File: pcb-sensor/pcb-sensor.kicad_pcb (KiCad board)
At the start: 2 copper layers, 84 x 84 mm, 13 parts, among them J1 Conn_02x06_Counter_Clockwise, J2 Conn_01x10, U1 4N25, U2 LT1962-5

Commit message: sensor pcb
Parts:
- added D3: D, Diode_SMD:D_1206_3216Metric_Pad1.42x1.75mm_HandSolder, F.Cu at (135.0, 98.5)
- added J3: Conn_01x02, Connector_PinSocket_2.54mm:PinSocket_2x01_P2.54mm_Vertical, F.Cu at (176.6, 103.3)
- added R10: R, Resistor_SMD:R_1206_3216Metric_Pad1.30x1.75mm_HandSolder, F.Cu at (144.0, 81.5)
- added R11: R, Resistor_SMD:R_1206_3216Metric_Pad1.30x1.75mm_HandSolder, F.Cu at (160.0, 88.5)
- added R12: R, Resistor_SMD:R_1206_3216Metric_Pad1.30x1.75mm_HandSolder, F.Cu at (178.6, 97.3)
- added R7: R, Resistor_SMD:R_1206_3216Metric_Pad1.30x1.75mm_HandSolder, F.Cu at (148.0, 72.5)
- added R8: R, Resistor_SMD:R_1206_3216Metric_Pad1.30x1.75mm_HandSolder, F.Cu at (143.9, 65.5)
- added R9: R, Resistor_SMD:R_1206_3216Metric_Pad1.30x1.75mm_HandSolder, F.Cu at (158.9, 65.5)
- added U3: 4N35, footprints:4N35S, F.Cu at (153.5, 69.0)
- added U4: 4N35, footprints:4N35S, F.Cu at (138.5, 85.0)
- added U5: TLSM, footprints:TLSM, F.Cu at (187.5, 100.3)
- J2: value Conn_01x10 -> Conn_01x12; footprint Connector_JST:JST_XH_S10B-XH-A_1x10_P2.50mm_Horizontal -> Connector_PinHeader_2.54mm:PinHeader_1x12_P2.54mm_Vertical
- U1: value 4N25 -> LM340MP; footprint Package_DIP:DIP-6_W7.62mm -> Package_TO_SOT_SMD:SOT-223
- U2: value LT1962-5 -> 4N35; footprint Package_SO:MSOP-8_3x3mm_P0.65mm -> footprints:4N35S
- moved U1 65.1 mm to (177.8, 116.0)
- moved U2 63.8 mm to (138.5, 69.0), turned to 0 degrees
- moved C1 29.2 mm to (135.0, 104.6)
- moved R6 28.7 mm to (131.0, 104.5)
- moved J2 28.1 mm to (136.0, 122.0), turned to 90 degrees
- moved R3 23.7 mm to (152.0, 88.5), turned to 270 degrees
- moved R2 22.8 mm to (156.0, 88.5), turned to 270 degrees
- moved R5 20.9 mm to (131.0, 98.5), turned to 270 degrees
- moved R4 20.3 mm to (133.0, 72.5), turned to 270 degrees
- moved R1 17.0 mm to (133.0, 88.5)
- moved D1 14.2 mm to (131.5, 83.0), turned to 180 degrees
- moved D2 11.3 mm to (131.5, 80.0), turned to 180 degrees
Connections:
- net /TURN_SIGNAL_LEFT_12V renamed /TURN_SIGNAL_LEFT
- net /TURN_SIGNAL_RIGHT_12V renamed /TURN_SIGNAL_RIGHT
- C1 pad 1: /ADC6 -> /ADC7
- D1 pad 1: /PD5 -> Net-(D1-Pad1)
- D2 pad 1: /PD5 -> Net-(D1-Pad1)
- J1 pad 1: /HIGH_BEAM_12V -> /PD4
- J1 pad 5: /NEUTRAL_12V -> /PD2
- J1 pad 6: /PD7 -> /NEUTRAL
- J1 pad 7: +5V -> /PD1
- J2 pad 10: /TACHO_12V -> /PD2
- J2 pad 4: /HIGH_BEAM_12V -> /HIGH_BEAM
- J2 pad 5: /NEUTRAL_12V -> /NEUTRAL
- J2 pad 6: /OIL_PRESSURE_12V -> /OIL_PRESSURE
- J2 pad 9: /SPEEDO_12V -> /COIL
- R1 pad 1: /PD5 -> Net-(D1-Pad1)
- R1 pad 2: GND -> Net-(R1-Pad2)
- R2 pad 2: /NEUTRAL_12V -> /NEUTRAL
- R4 pad 1: /HIGH_BEAM_12V -> /HIGH_BEAM
- R4 pad 2: GND -> Net-(R4-Pad2)
- R5 pad 2: /ADC6 -> /ADC7
- R6 pad 1: /ADC6 -> /ADC7
- U1 pad 1: /KEY_12V -> +12V
- U1 pad 2: /TACHO_12V -> GND
- U1 pad 3: Net-(U1-Pad3) -> +5V
- U2 pad 1: +5V -> Net-(R4-Pad2)
- U2 pad 2: Net-(U2-Pad2) -> GND
- U2 pad 5: Net-(U2-Pad5) -> /PD4
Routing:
- net +5V: track 0.00 -> 96.1 mm
- net /ADC7: track 0.00 -> 56.8 mm
- net /PD4: track 0.00 -> 41.2 mm
- net /PD1: track 0.00 -> 40.3 mm
- net GND: track 3.13 -> 37.5 mm, vias 1 -> 7
- net /PD6: track 0.00 -> 34.1 mm
- net /OIL_PRESSURE_12V: track 0.00 -> 34.1 mm
- net /PD2: track 0.00 -> 25.0 mm
- net /NEUTRAL: track 0.00 -> 24.0 mm
- net /ADC6: track 10.0 -> 0.00 mm
- net /PD5: track 10.0 -> 18.1 mm
- net Net-(D1-Pad1): track 0.00 -> 6.90 mm
- net Net-(R7-Pad2): track 0.00 -> 3.00 mm
- net Net-(R4-Pad2): track 0.00 -> 3.00 mm
- net Net-(R1-Pad2): track 0.00 -> 3.00 mm
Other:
- board text added: "BATT_12V"
- board text added: "COIL"
- board text added: "GND"
- board text added: "HIGH_BEAM"
- board text added: "KEY_12V"
- board text added: "NEUTRAL"
- board text added: "OIL_PRES"
- board text added: "SPEED_5V"
- board text added: "SPEED_GND"
- board text added: "SPEED_OUT"
- board text added: "TURN_LEFT"
- board text added: "TURN_RIGHT"

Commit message: v1.0
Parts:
- moved U5 2.52 mm to (185.0, 100.0)
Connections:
- J1 pad 3: /OIL_PRESSURE_12V -> /OIL_PRESSURE
- J2 pad 2: +12V -> /HIGH_BEAM
- J2 pad 3: /KEY_12V -> /TURN_SIGNAL_RIGHT
- J2 pad 4: /HIGH_BEAM -> /TURN_SIGNAL_LEFT
- J2 pad 5: /NEUTRAL -> /KEY_12V
- J2 pad 7: /TURN_SIGNAL_RIGHT -> /NEUTRAL
- J2 pad 8: /TURN_SIGNAL_LEFT -> /COIL
- J2 pad 9: /COIL -> +12V
- R3 pad 2: /OIL_PRESSURE_12V -> /OIL_PRESSURE
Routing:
- net /OIL_PRESSURE: track 0.00 -> 74.8 mm, vias 0 -> 1
- net /KEY_12V: track 0.00 -> 67.4 mm, vias 0 -> 2
- net /HIGH_BEAM: track 0.00 -> 60.3 mm, vias 0 -> 1
- net +5V: track 96.1 -> 150.1 mm, vias 0 -> 3
- net /COIL: track 0.00 -> 52.0 mm, vias 0 -> 1
- net /TURN_SIGNAL_RIGHT: track 0.00 -> 50.7 mm, vias 0 -> 1
- net /TURN_SIGNAL_LEFT: track 0.00 -> 48.4 mm, vias 0 -> 1
- net /NEUTRAL: track 24.0 -> 62.4 mm, vias 0 -> 1
- net /PD2: track 25.0 -> 60.3 mm, vias 0 -> 1
- net /OIL_PRESSURE_12V: track 34.1 -> 0.00 mm
- net +12V: track 0.00 -> 24.0 mm, vias 0 -> 1
- net GND: track 37.5 -> 40.0 mm, vias 7 -> 8
- net /ADC7: track 56.8 -> 55.1 mm
- net /PD1: track 40.3 -> 39.5 mm
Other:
- outline, holes or cut-outs redrawn
- board text added: "5V"
- board text added: "ADC6"
- board text added: "ADC7"
- board text added: "JLCJLCJLCJLC"
- board text added: "Motorcycle Tacho v1.0"
- board text added: "PB0"
- board text added: "PD1"
- board text added: "PD2"
- board text added: "PD3"
- board text added: "PD4"
- board text added: "PD5"
- board text added: "PD6"
- board text added: "PD7"

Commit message: add oshw logo
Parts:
- added G***: LOGO, footprints:OSHW, F.Cu at (128.0, 127.8)

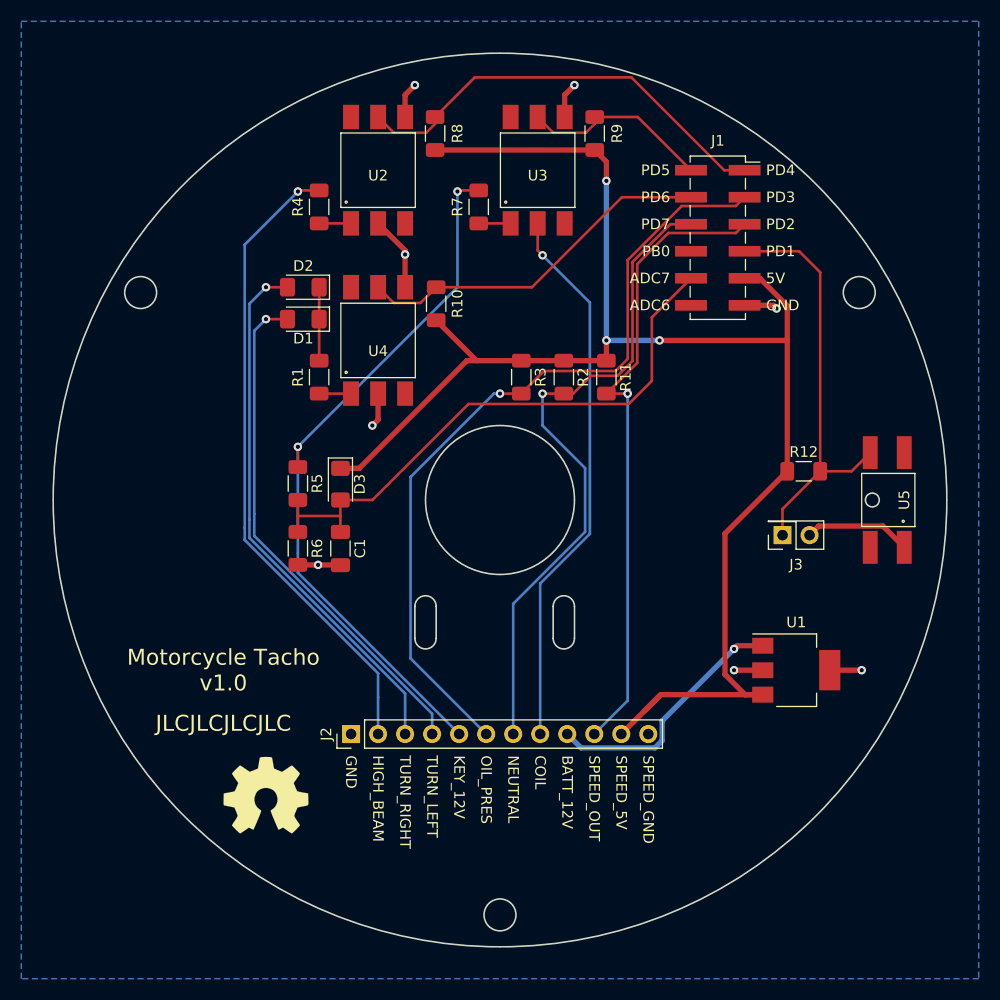
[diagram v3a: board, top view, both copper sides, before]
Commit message: made pcb bigger
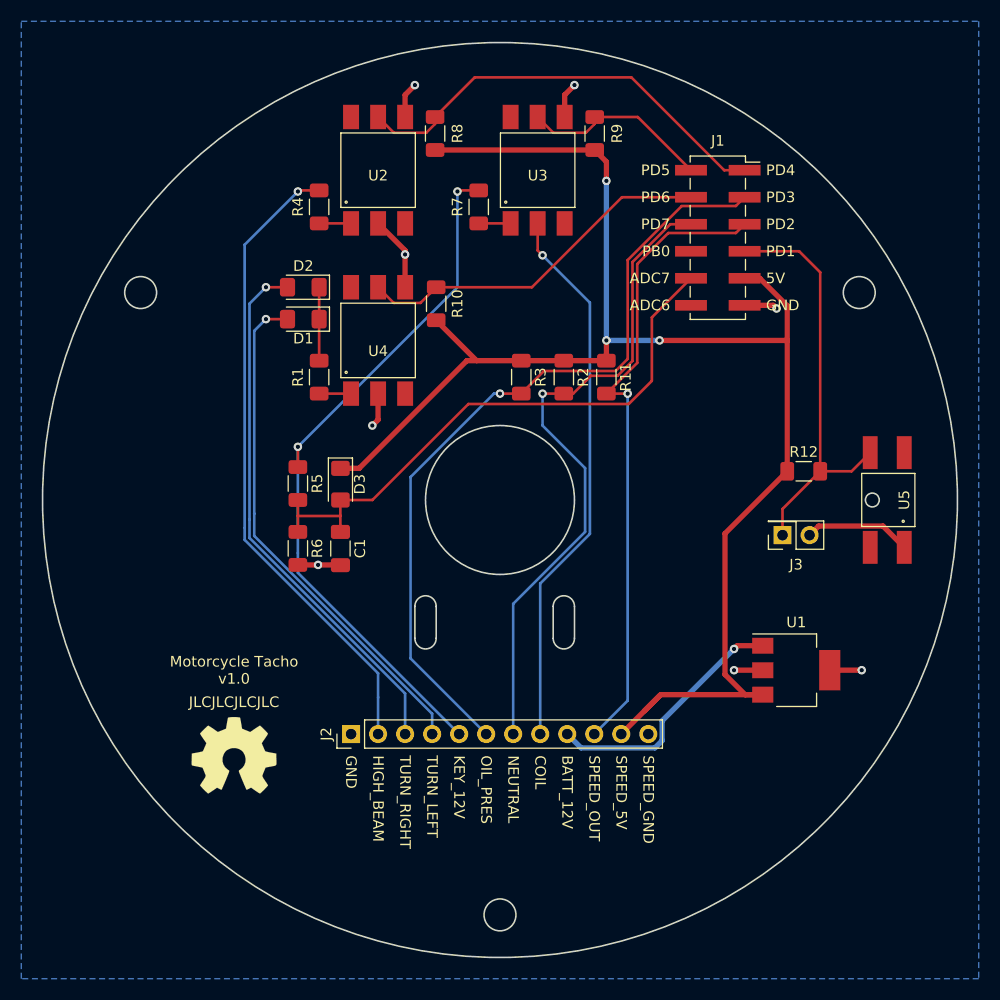
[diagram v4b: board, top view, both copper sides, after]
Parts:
- moved G*** 4.80 mm to (125.0, 124.0)
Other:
- board size 84 x 84 mm -> 86 x 86 mm
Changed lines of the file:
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@@
   )
   (module footprints:OSHW (layer F.Cu)
-    (at 128 127.75)
+    (at 125 124)
     (fp_text reference G*** (at 0 0) (layer F.SilkS) hide
       (effects (font (size 1.524 1.524) (thickness 0.3)))
@@
     )
   )
-  (gr_text JLCJLCJLCJLC (at 124 121) (layer F.SilkS)
-    (effects (font (size 1.5 1.5) (thickness 0.3)))
-  )
-  (gr_text "Motorcycle Tacho\nv1.0" (at 124 116) (layer F.SilkS)
-    (effects (font (size 1.5 1.5) (thickness 0.3)))
+  (gr_text JLCJLCJLCJLC (at 125 119) (layer F.SilkS)
+    (effects (font (size 1 1) (thickness 0.15)))
+  )
+  (gr_text "Motorcycle Tacho\nv1.0" (at 125 116) (layer F.SilkS)
+    (effects (font (size 1 1) (thickness 0.15)))
   )
   (gr_circle (center 185 100) (end 185.65 100) (layer Edge.Cuts) (width 0.15))
@@
   (gr_circle (center 116.22 80.5) (end 117.72 80.5) (layer Edge.Cuts) (width 0.15))
   (gr_circle (center 150 139) (end 151.5 139) (layer Edge.Cuts) (width 0.15))
-  (gr_circle (center 150 100) (end 192 100) (layer Edge.Cuts) (width 0.15))
+  (gr_circle (center 150 100) (end 193 100) (layer Edge.Cuts) (width 0.15))
   (via (at 176 82) (size 0.8) (drill 0.4) (layers F.Cu B.Cu) (net 2))
   (segment (start 175.7 81.7) (end 176 82) (width 0.5) (layer F.Cu) (net 2))

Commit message: started v1.1
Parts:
- removed G***: LOGO, footprints:OSHW
- removed R12: R, Resistor_SMD:R_1206_3216Metric_Pad1.30x1.75mm_HandSolder
- removed U5: TLSM, footprints:TLSM
- added C2: CP, Capacitor_THT:CP_Radial_D8.0mm_P3.80mm, F.Cu at (175.0, 102.0)
- added C3: 0.22u, Capacitor_SMD:C_1206_3216Metric_Pad1.33x1.80mm_HandSolder, F.Cu at (176.6, 109.0)
- added C4: 0.1u, Capacitor_SMD:C_1206_3216Metric_Pad1.33x1.80mm_HandSolder, F.Cu at (176.6, 122.0)
- added D4: 1N4148, Diode_SMD:D_1206_3216Metric_Pad1.42x1.75mm_HandSolder, F.Cu at (169.5, 102.0)
- added J4: Conn_01x05, Connector_PinSocket_2.54mm:PinSocket_1x05_P2.54mm_Vertical, F.Cu at (139.0, 126.0)
- added J5: Conn_01x02, Connector_PinSocket_2.54mm:PinSocket_1x02_P2.54mm_Vertical, F.Cu at (130.0, 130.0)
- added J6: Conn_01x03, Connector_PinSocket_2.54mm:PinSocket_1x03_P2.54mm_Vertical, F.Cu at (154.0, 133.0)
- D1, D2: value D -> 1N4148
- J1: footprint Connector_PinSocket_2.54mm:PinSocket_2x06_P2.54mm_Vertical_SMD -> Connector_PinSocket_2.54mm:PinSocket_2x06_P2.54mm_Vertical
- J2: value Conn_01x12 -> Conn_01x03; footprint Connector_PinHeader_2.54mm:PinHeader_1x12_P2.54mm_Vertical -> Connector_PinSocket_2.54mm:PinSocket_1x03_P2.54mm_Vertical
- J3: footprint Connector_PinSocket_2.54mm:PinSocket_2x01_P2.54mm_Vertical -> Connector_PinSocket_2.54mm:PinSocket_1x02_P2.54mm_Vertical
- R1, R4: value R -> 1k
- R10, R8: value R -> 200
- R2, R3: value R -> 10k
- moved J3 26.3 mm to (171.0, 129.0)
- moved J2 23.3 mm to (159.0, 126.0)
- moved J1 6.52 mm to (169.0, 69.0)
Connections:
- J1 pad 7: /PD1 -> /MODE_BUTTON
- J2 pad 1: GND -> /PD2
- J2 pad 2: /HIGH_BEAM -> +5V
- J2 pad 3: /TURN_SIGNAL_RIGHT -> GND
- J3 pad 1: /PD1 -> GND
- J3 pad 2: GND -> /MODE_BUTTON
- R5 pad 1: /KEY_12V -> +12V
- R7 pad 1: /KEY_12V -> +12V
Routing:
- net +5V: track 150.1 -> 53.4 mm, vias 3 -> 0
- net /KEY_12V: track 67.4 -> 0.00 mm, vias 2 -> 0
- net +12V: track 24.0 -> 83.7 mm, vias 1 -> 2
- net /PD1: track 39.5 -> 0.00 mm
- net GND: track 40.0 -> 21.0 mm, vias 8 -> 5
- net /PD4: track 41.2 -> 37.5 mm
- net /PD6: track 34.1 -> 32.6 mm
- net /PD5: track 18.1 -> 16.6 mm
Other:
- board size 86 x 86 mm -> 84 x 84 mm
- board text added: "Motorcycle Tacho v1.1"
- board text removed: "Motorcycle Tacho v1.0"

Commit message: more v1.1
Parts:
- removed R7, R9: R, Resistor_SMD:R_1206_3216Metric_Pad1.30x1.75mm_HandSolder
- removed U3: 4N35, footprints:4N35S
- added J7: Conn_01x01, Connector_PinSocket_2.54mm:PinSocket_1x01_P2.54mm_Vertical, F.Cu at (178.0, 81.8)
- added J8: Conn_01x01, Connector_PinSocket_2.54mm:PinSocket_1x01_P2.54mm_Vertical, F.Cu at (178.0, 77.0)
- J3: value Conn_01x02 -> Conn_01x01; footprint Connector_PinSocket_2.54mm:PinSocket_1x02_P2.54mm_Vertical -> Connector_PinSocket_2.54mm:PinSocket_1x01_P2.54mm_Vertical
- R10, R8: value 200 -> 10k
- U2, U4: value 4N35 -> SFH617A-1; footprint footprints:4N35S -> Package_SO:SOP-4_4.4x2.6mm_P1.27mm
- moved R6 56.1 mm to (187.1, 103.5), turned to 0 degrees
- moved C1 52.4 mm to (187.1, 98.5), turned to 0 degrees
- moved R2 50.6 mm to (142.0, 137.1), turned to 90 degrees
- moved R5 50.2 mm to (180.9, 103.5), turned to 0 degrees
- moved R3 50.2 mm to (139.5, 137.1), turned to 90 degrees
- moved R11 48.9 mm to (155.0, 137.1), turned to 90 degrees
- moved D3 46.0 mm to (181.0, 98.5), turned to 0 degrees
- moved J5 34.4 mm to (164.0, 125.0), turned to 90 degrees
- moved C4 27.2 mm to (173.4, 95.0), turned to 180 degrees
- moved D4 22.2 mm to (175.0, 123.5), turned to 270 degrees
- moved U1 16.0 mm to (172.2, 101.0), turned to 180 degrees
- moved J6 14.4 mm to (142.0, 125.0), turned to 90 degrees
- moved C2 13.0 mm to (175.0, 115.0), turned to 180 degrees
- moved J3 11.7 mm to (160.0, 125.0), turned to 0 degrees
- moved J4 11.0 mm to (128.0, 125.0)
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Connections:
- J1 pad 4: /PD6 -> /NEUTRAL
- J1 pad 6: /NEUTRAL -> /PD7
- J2 pad 1: /PD2 -> /PD7
- J2 pad 2: +5V -> +12V
- J3 pad 1: GND -> /MODE_BUTTON
- J6 pad 2: Net-(J6-Pad2) -> +12V
- J6 pad 3: /COIL -> /PD2
- R10 pad 2: /PD6 -> /PD5
- R11 pad 2: /PD2 -> /PD7
- U2 pad 3: Net-(U2-Pad3) -> GND
- U2 pad 4: GND -> /PD4
- U4 pad 3: Net-(U4-Pad3) -> GND
- U4 pad 4: GND -> /PD5
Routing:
- net +5V: track 53.4 -> 135.0 mm, vias 0 -> 2
- net /PD7: track 0.00 -> 70.3 mm
- net /MODE_BUTTON: track 0.00 -> 55.6 mm
- net /COIL: track 52.0 -> 0.00 mm, vias 1 -> 0
- net /PD6: track 32.6 -> 0.00 mm
- net GND: track 21.0 -> 49.7 mm, vias 5 -> 4
- net /NEUTRAL: track 62.4 -> 82.4 mm, vias 1 -> 0
- net +12V: track 83.7 -> 66.4 mm, vias 2 -> 0
- net /ADC7: track 55.1 -> 41.1 mm
- net /PB0: track 0.00 -> 12.5 mm
- net /ADC6: track 0.00 -> 12.5 mm
- net /PD5: track 16.6 -> 27.6 mm
- net /OIL_PRESSURE: track 74.8 -> 85.4 mm, vias 1 -> 0
- net /PD4: track 37.5 -> 27.4 mm
- net Net-(D4-Pad2): track 0.00 -> 8.46 mm
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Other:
- board text added: "12V"
- board text added: "MODE_BUTTON"
- board text added: "SPEED"
- board text added: "SPEED_12V"
- board text added: "TACH"
- board text added: "TACH_12V"
- board text added: "TACH_GND"
- board text removed: "BATT_12V"
- board text removed: "COIL"
- board text removed: "KEY_12V"
- board text removed: "SPEED_5V"
- board text removed: "SPEED_OUT"

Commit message: v1.1
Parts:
- C1: value C -> 100n
- C2: value CP -> 100u
- D1, D2, D4: value 1N4148 -> 1N4001
- D3: value D -> 1N4001
- R11, R5: value R -> 10k
- R6: value R -> 4.7k
- moved J2 1.50 mm to (151.0, 123.5)
- moved J3 1.50 mm to (160.0, 123.5)
- moved J4 1.50 mm to (128.0, 123.5)
- moved J5 1.50 mm to (164.0, 123.5)
- moved J6 1.50 mm to (142.0, 123.5)
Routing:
- net +12V: track 66.4 -> 71.0 mm
- net /TURN_SIGNAL_LEFT: track 44.5 -> 43.0 mm
- net /TURN_SIGNAL_RIGHT: track 48.7 -> 47.2 mm
- net /MODE_BUTTON: track 55.6 -> 54.1 mm
- net /HIGH_BEAM: track 61.1 -> 59.6 mm
- net /PD2: track 64.0 -> 63.3 mm
- net Net-(D4-Pad2): track 8.46 -> 9.08 mm
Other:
- board size 84 x 84 mm -> 86 x 86 mm

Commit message: migrate to kicad 6
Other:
- net class Default removed
